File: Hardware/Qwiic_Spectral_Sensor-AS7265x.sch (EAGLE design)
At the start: 48 parts, among them J1 SMD, J2 Serial Interface, J4 SMD, J5 Flash Programming, J8 PTH, U1 AS72651, U3 4MB Flash, U5 AS72653, U6 AS72652

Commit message: Updating with Buzzard labels. Change logo to SparkFun. Change v to v10.
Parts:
- removed U$1: SPARKX-LOGO3, SparkX:SPARKX-LOGO3
- added FD3, FD4: FIDUCIAL1X2, SparkFun-Aesthetics:FIDUCIAL1X2
- added LOGO1: SFE_LOGO_NAME_FLAME.1_INCH, SparkFun-Aesthetics:SFE_LOGO_NAME_FLAME.1_INCH
- BULB1, BULB2, BULB3: value Incandescent -> LEDNS
- D5: device SparkX:LEDPLCC -> SparkX:LEDLD
- JP1: value JUMPER-SMT_3_2-NC_PASTE_SILK -> JUMPER-SMT_3_2-NC_TRACE_SILK; device SparkFun-Jumpers:JUMPER-SMT_3_2-NC_PASTE_SILK -> SparkFun-Jumpers:JUMPER-SMT_3_2-NC_TRACE_SILK
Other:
- note removed: "13lm"
- moved on the sheet: U3

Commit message: Removing old files
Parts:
- D3: device SparkFun-LED:LED0603 -> SparkFun-LED:LED-IR0603
- D5: device SparkX:LEDLD -> SparkFun-LED:LED-UVPLCC
- J1, J4: value SMD -> (none); device SparkX:I2C_STANDARDJS-1MM -> SparkFun-Connectors:QWIIC_CONNECTORJS-1MM
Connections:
- net 3.3V: now also J1.2, J4.2; no longer J1.VCC, J4.VCC
- net GND: now also J1.1, J4.1; no longer J1.GND, J4.GND
- net RX/SCL: now also J1.4, J4.4; no longer J1.SCL, J4.SCL
- net TX/SDA: now also J1.3, J4.3; no longer J1.SDA, J4.SDA
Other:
- note added: "The AS7261 must be held in reset while programming flash"
- note removed: "The AS726x must be held in reset while programming flash"

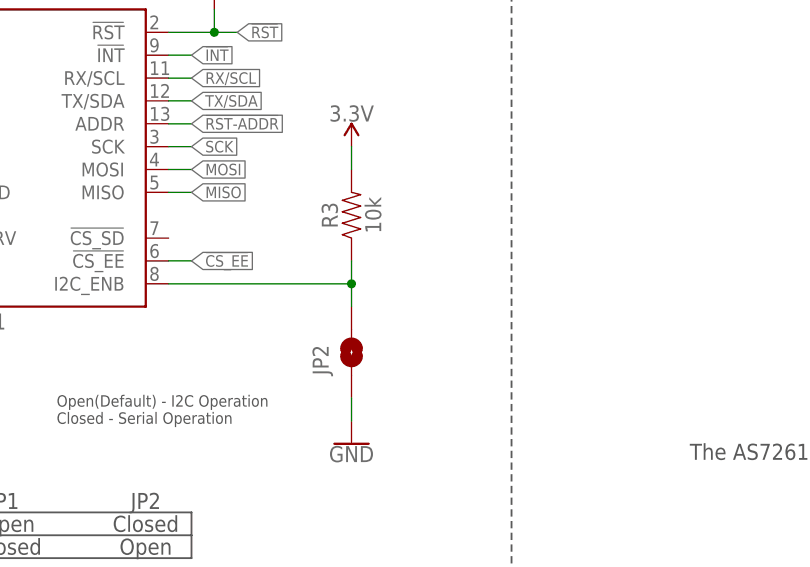
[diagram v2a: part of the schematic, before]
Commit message: Adding prod_ids to new parts
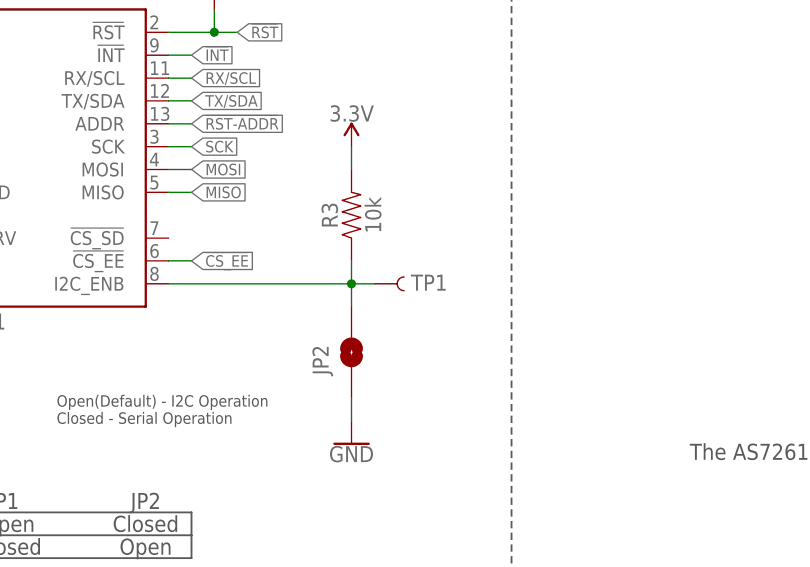
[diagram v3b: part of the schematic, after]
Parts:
- added TP1: TEST-POINT3, SparkFun-Connectors:TEST-POINT3
- U1: device AS7265x:AS7265X -> Qwiic_Spectral_Sensor-AS7265x:AS72651
- U5: device AS7265x:AS72652/53 -> Qwiic_Spectral_Sensor-AS7265x:AS72653
- U6: device AS7265x:AS72652/53 -> Qwiic_Spectral_Sensor-AS7265x:AS72652
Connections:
- net I2C_ENB: now also TP1.1
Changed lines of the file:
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@@
 <part name="FD1" library="SparkFun-Aesthetics" deviceset="FIDUCIAL" device="1X2"/>
 <part name="FD2" library="SparkFun-Aesthetics" deviceset="FIDUCIAL" device="1X2"/>
-<part name="U1" library="AS7265x" deviceset="AS7265X" device="" value="AS72651"/>
+<part name="U1" library="Qwiic_Spectral_Sensor-AS7265x" deviceset="AS72651" device="" value="AS72651"/>
 <part name="GND2" library="SparkFun-PowerSymbols" deviceset="GND" device=""/>
 <part name="SUPPLY1" library="SparkFun-PowerSymbols" deviceset="3.3V" device=""/>
@@
 <part name="R8" library="SparkFun-Resistors" deviceset="10KOHM" device="-0603-1/10W-1%" value="10k"/>
 <part name="GND21" library="SparkFun-PowerSymbols" deviceset="GND" device=""/>
-<part name="U5" library="AS7265x" deviceset="AS72652/53" device="" value="AS72653"/>
-<part name="U6" library="AS7265x" deviceset="AS72652/53" device="" value="AS72652"/>
+<part name="U5" library="Qwiic_Spectral_Sensor-AS7265x" deviceset="AS72653" device="" value="AS72653"/>
+<part name="U6" library="Qwiic_Spectral_Sensor-AS7265x" deviceset="AS72652" device="" value="AS72652"/>
 <part name="JP5" library="SparkFun-Jumpers" deviceset="JUMPER-SMT_2_NC_TRACE" device="_NO-SILK" value=""/>
 <part name="JP3" library="SparkFun-Jumpers" deviceset="JUMPER-SMT_2_NC_TRACE" device="_NO-SILK" value=""/>
@@
 <part name="D5" library="SparkFun-LED" deviceset="LED-UV" device="PLCC" value="UV"/>
 <part name="D3" library="SparkFun-LED" deviceset="LED-IR" device="0603" value="IR"/>
+<part name="TP1" library="SparkFun-Connectors" deviceset="TEST-POINT" device="3" value=""/>
 </parts>
 <sheets>
@@
 <attribute name="VALUE" x="424.18" y="98.806" size="1.778" layer="96" align="top-center"/>
 </instance>
-<instance part="U5" gate="U" x="406.4" y="124.46">
+<instance part="U5" gate="U1" x="406.4" y="124.46">
 <attribute name="NAME" x="393.7" y="143.002" size="1.778" layer="95"/>
 <attribute name="VALUE" x="393.7" y="106.68" size="1.778" layer="96"/>
 </instance>
-<instance part="U6" gate="U" x="309.88" y="127">
+<instance part="U6" gate="U1" x="309.88" y="127">
 <attribute name="NAME" x="297.18" y="145.542" size="1.778" layer="95"/>
 <attribute name="VALUE" x="297.18" y="109.22" size="1.778" layer="96"/>
@@
 </instance>
 <instance part="D3" gate="G$1" x="284.48" y="142.24"/>
+<instance part="TP1" gate="G$1" x="114.3" y="116.84" smashed="yes">
+<attribute name="NAME" x="118.364" y="116.078" size="1.778" layer="95" font="vector"/>
+<attribute name="VALUE" x="111.76" y="114.3" size="1.778" layer="96" font="vector"/>
+</instance>
 </instances>
 <busses>
@@
 <wire x1="292.1" y1="114.3" x2="292.1" y2="111.76" width="0.1524" layer="91"/>
 <pinref part="GND13" gate="1" pin="GND"/>
-<pinref part="U6" gate="U" pin="GND"/>
+<pinref part="U6" gate="U1" pin="GND"/>
 </segment>
 <segment>
@@
 <wire x1="388.62" y1="111.76" x2="388.62" y2="109.22" width="0.1524" layer="91"/>
 <pinref part="GND19" gate="1" pin="GND"/>
-<pinref part="U5" gate="U" pin="GND"/>
+<pinref part="U5" gate="U1" pin="GND"/>
 </segment>
 <segment>
@@
 <wire x1="292.1" y1="142.24" x2="292.1" y2="144.78" width="0.1524" layer="91"/>
 <pinref part="SUPPLY19" gate="G$1" pin="3.3V"/>
-<pinref part="U6" gate="U" pin="VDD"/>
+<pinref part="U6" gate="U1" pin="VDD"/>
 </segment>
 <segment>
@@
 <wire x1="388.62" y1="139.7" x2="388.62" y2="142.24" width="0.1524" layer="91"/>
 <pinref part="SUPPLY27" gate="G$1" pin="3.3V"/>
-<pinref part="U5" gate="U" pin="VDD"/>
+<pinref part="U5" gate="U1" pin="VDD"/>
 </segment>
 <segment>
@@
 <wire x1="421.64" y1="139.7" x2="424.18" y2="139.7" width="0.1524" layer="91"/>
 <label x="424.18" y="139.7" size="1.27" layer="95" xref="yes"/>
-<pinref part="U5" gate="U" pin="!RST"/>
+<pinref part="U5" gate="U1" pin="!RST"/>
 </segment>
 </net>
@@
 <junction x="111.76" y="116.84"/>
 <pinref part="R3" gate="G$1" pin="1"/>
+<wire x1="111.76" y1="116.84" x2="114.3" y2="116.84" width="0.1524" layer="91"/>
+<pinref part="TP1" gate="G$1" pin="1"/>
 </segment>
 </net>
@@
 <wire x1="284.48" y1="119.38" x2="284.48" y2="129.54" width="0.1524" layer="91"/>
 <junction x="284.48" y="129.54"/>
-<pinref part="U6" gate="U" pin="LED_DRV"/>
+<pinref part="U6" gate="U1" pin="LED_DRV"/>
 <pinref part="D3" gate="G$1" pin="C"/>
 </segment>
@@
 <wire x1="325.12" y1="137.16" x2="327.66" y2="137.16" width="0.1524" layer="91"/>
 <label x="327.66" y="137.16" size="1.27" layer="95" xref="yes"/>
-<pinref part="U6" gate="U" pin="SCL_S"/>
+<pinref part="U6" gate="U1" pin="SCL_S"/>
 </segment>
 <segment>
@@
 <wire x1="421.64" y1="134.62" x2="424.18" y2="134.62" width="0.1524" layer="91"/>
 <label x="424.18" y="134.62" size="1.27" layer="95" xref="yes"/>
-<pinref part="U5" gate="U" pin="SCL_S"/>
+<pinref part="U5" gate="U1" pin="SCL_S"/>
 </segment>
 </net>
@@
 <wire x1="325.12" y1="134.62" x2="327.66" y2="134.62" width="0.1524" layer="91"/>
 <label x="327.66" y="134.62" size="1.27" layer="95" xref="yes"/>
-<pinref part="U6" gate="U" pin="SDA_S"/>
+<pinref part="U6" gate="U1" pin="SDA_S"/>
 </segment>
 <segment>
@@
 <wire x1="421.64" y1="132.08" x2="424.18" y2="132.08" width="0.1524" layer="91"/>
 <label x="424.18" y="132.08" size="1.27" layer="95" xref="yes"/>
-<pinref part="U5" gate="U" pin="SDA_S"/>
+<pinref part="U5" gate="U1" pin="SDA_S"/>
 </segment>
 </net>
@@
 <wire x1="325.12" y1="119.38" x2="327.66" y2="119.38" width="0.1524" layer="91"/>
 <wire x1="327.66" y1="119.38" x2="327.66" y2="116.84" width="0.1524" layer="91"/>
-<pinref part="U6" gate="U" pin="!CS_SD"/>
+<pinref part="U6" gate="U1" pin="!CS_SD"/>
 </segment>
 </net>
@@
 <wire x1="325.12" y1="124.46" x2="335.28" y2="124.46" width="0.1524" layer="91"/>
 <wire x1="335.28" y1="124.46" x2="335.28" y2="116.84" width="0.1524" layer="91"/>
-<pinref part="U6" gate="U" pin="MISO"/>
+<pinref part="U6" gate="U1" pin="MISO"/>
 </segment>
 </net>
@@
 <wire x1="325.12" y1="142.24" x2="327.66" y2="142.24" width="0.1524" layer="91"/>
 <label x="327.66" y="142.24" size="1.27" layer="95" xref="yes"/>
-<pinref part="U6" gate="U" pin="!RST"/>
+<pinref part="U6" gate="U1" pin="!RST"/>
 </segment>
 <segment>
@@
 <wire x1="391.16" y1="116.84" x2="381" y2="116.84" width="0.1524" layer="91"/>
 <wire x1="381" y1="116.84" x2="381" y2="127" width="0.1524" layer="91"/>
-<pinref part="U5" gate="U" pin="LED_DRV"/>
+<pinref part="U5" gate="U1" pin="LED_DRV"/>
 <wire x1="381" y1="134.62" x2="381" y2="127" width="0.1524" layer="91"/>
 <junction x="381" y="127"/>
@@
 <wire x1="421.64" y1="116.84" x2="424.18" y2="116.84" width="0.1524" layer="91"/>
 <wire x1="424.18" y1="116.84" x2="424.18" y2="114.3" width="0.1524" layer="91"/>
-<pinref part="U5" gate="U" pin="!CS_SD"/>
+<pinref part="U5" gate="U1" pin="!CS_SD"/>
 </segment>
 </net>
@@
 <wire x1="421.64" y1="121.92" x2="431.8" y2="121.92" width="0.1524" layer="91"/>
 <wire x1="431.8" y1="121.92" x2="431.8" y2="114.3" width="0.1524" layer="91"/>
-<pinref part="U5" gate="U" pin="MISO"/>
-</segment>
-</net>
+<pinref part="U5" gate="U1" pin="MISO"/>
+</segment>
+</net>
